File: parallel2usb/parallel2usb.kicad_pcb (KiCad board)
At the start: 4 copper layers, 87.9 x 53.6 mm, 49 parts, among them J1 DB25_Male_MountingHoles, J2 Conn_01x20, J3 Conn_01x03_Male, U1 SN74LVC8T245PW, U2 SN74LVC8T245PW, U3 SN74LVC8T245PW, U4 Pico

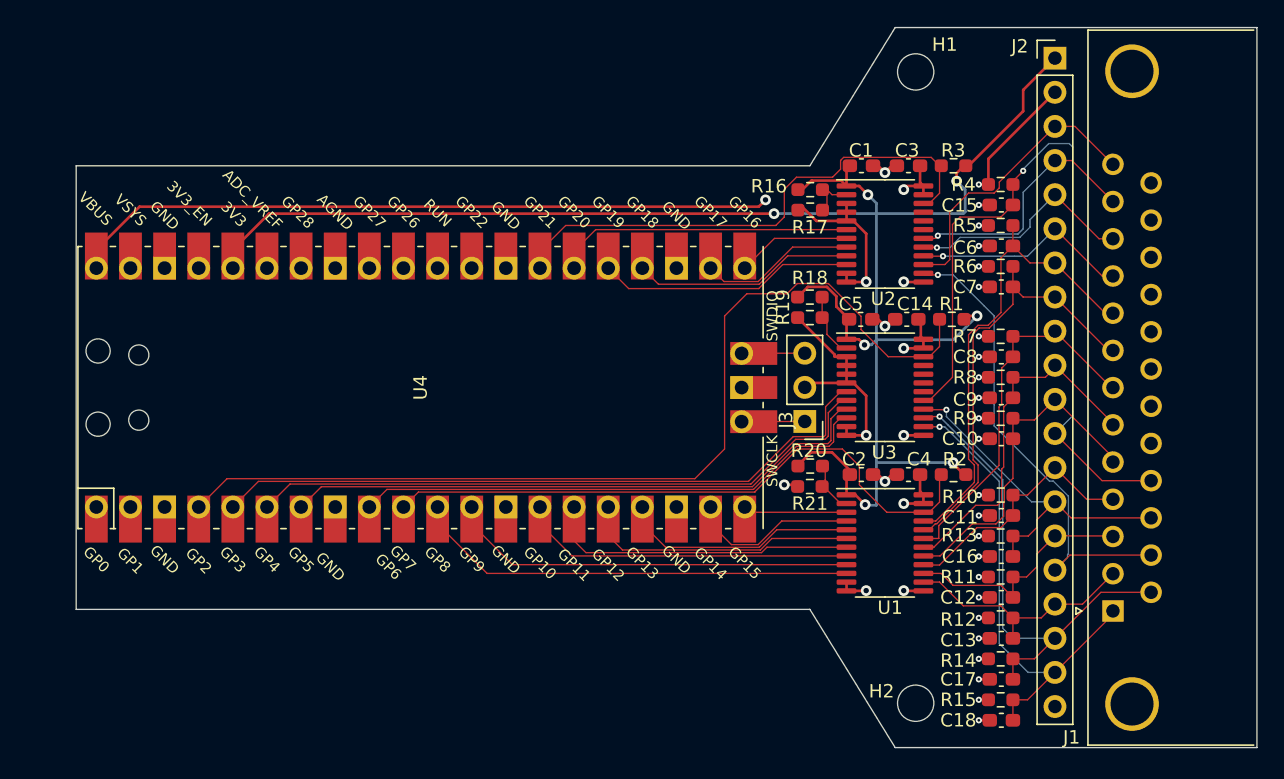
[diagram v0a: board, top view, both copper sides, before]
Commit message: Design with 74LVC161284.
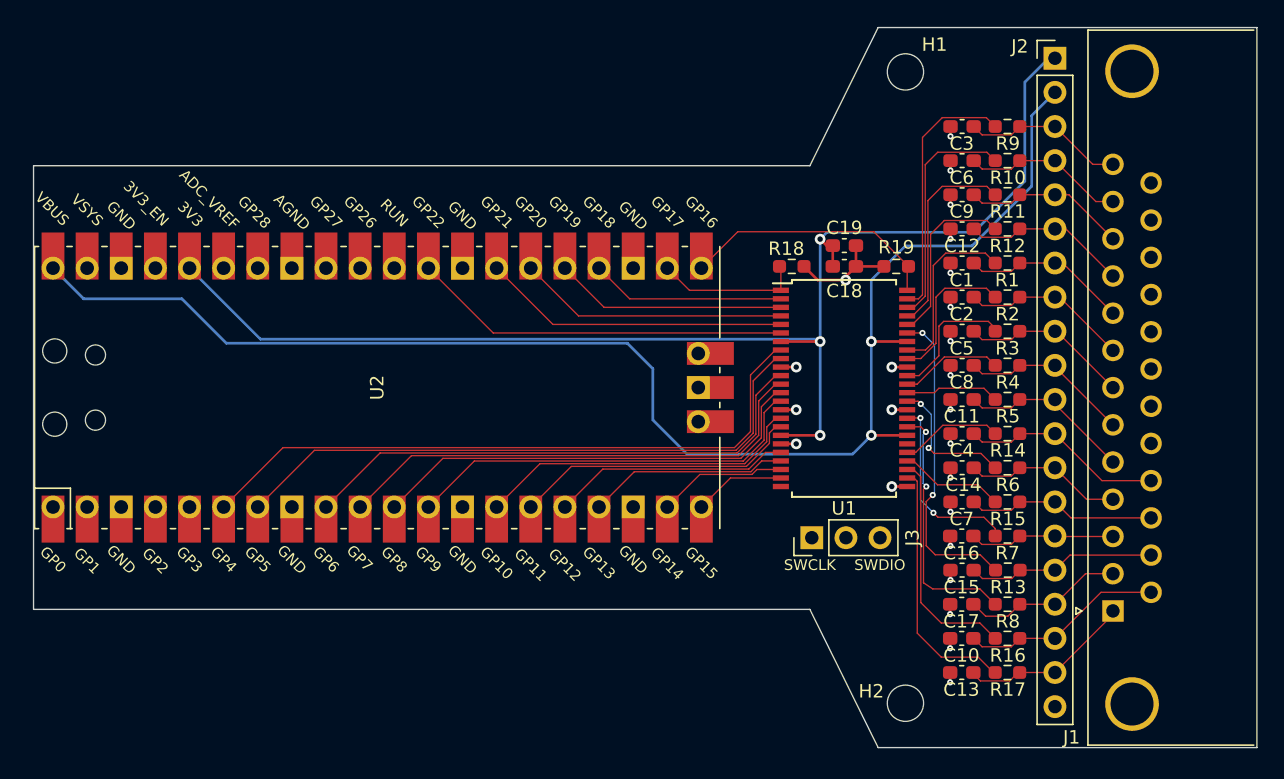
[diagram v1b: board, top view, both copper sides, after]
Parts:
- removed R20: NS, Resistor_SMD:R_0603_1608Metric_Pad0.98x0.95mm_HandSolder
- removed R21: 4K7, Resistor_SMD:R_0603_1608Metric_Pad0.98x0.95mm_HandSolder
- removed U3: SN74LVC8T245PW, Package_SO:TSSOP-24_4.4x7.8mm_P0.65mm
- removed U4: Pico, Raspberry Pico:RPi_Pico_SMD_TH
- added C19: 22u, Capacitor_SMD:C_0603_1608Metric_Pad1.08x0.95mm_HandSolder, F.Cu at (179.1, 91.0)
- C1, C10, C11, C12, C13, C14, C15, C16, C17, C2, C3, C4, C5, C6, C7, C8, C9: value 100n -> 100p
- R1, R10, R11, R12, R13, R14, R15, R16, R2, R3, R4, R5, R6, R7, R8, R9: value 4K7 -> 22
- R17: value NS -> 22
- R18: value NS -> 4K7
- U1: value SN74LVC8T245PW -> 74LVC161284DL; footprint Package_SO:TSSOP-24_4.4x7.8mm_P0.65mm -> Package_SO:SSOP-48_7.5x15.9mm_P0.635mm
- U2: value SN74LVC8T245PW -> Pico; footprint Package_SO:TSSOP-24_4.4x7.8mm_P0.65mm -> RPi_Pico:RPi_Pico_SMD_TH
- moved U2 39.5 mm to (144.3, 101.6), turned to 90 degrees
- moved R17 37.4 mm to (191.2, 122.8)
- moved R16 36.5 mm to (191.2, 120.3), turned to 180 degrees
- moved C18 35.7 mm to (179.1, 92.6), turned to 0 degrees
- moved R12 29.0 mm to (191.2, 89.8), turned to 180 degrees
- moved R11 28.5 mm to (191.2, 87.2), turned to 180 degrees
- moved C12 27.6 mm to (187.9, 89.8)
- moved C15 27.3 mm to (187.9, 115.2)
- moved R10 24.9 mm to (191.2, 84.7), turned to 180 degrees
- moved R9 21.7 mm to (191.2, 82.2), turned to 180 degrees
- moved R8 16.9 mm to (191.2, 117.7), turned to 180 degrees
- moved R14 16.8 mm to (191.2, 105.0), turned to 180 degrees
- moved C7 16.3 mm to (187.9, 110.1)
- moved C9 15.4 mm to (187.9, 87.2)
- moved C2 15.2 mm to (187.9, 94.9), turned to 180 degrees
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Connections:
- C1 pad 1: +3.3V -> /D7
- C10 pad 1: /D3 -> /AUTOF
- C11 pad 1: /D2 -> /D3
- C12 pad 1: /D1 -> /ACK
- C13 pad 1: /D0 -> /STROBE
- C14 pad 1: +5V -> /D2
- C15 pad 1: /SELIN -> /ERROR
- C16 pad 1: /INIT -> /D1
- C17 pad 1: /AUTOF -> /D0
- C18 pad 1: /STROBE -> Vcc
- C2 pad 1: +3.3V -> /D6
- C3 pad 1: +5V -> /SEL
- C4 pad 1: +5V -> /SELIN
- C5 pad 1: +3.3V -> /D5
- C6 pad 1: /D7 -> /PE
- C7 pad 1: /D6 -> /INIT
- C8 pad 1: /D5 -> /D4
- C9 pad 1: /D4 -> /BUSY
- J2 pad 1: +3.3V -> Vcc
- J2 pad 2: +5V -> Vcc_Cable
- R1 pad 1: +3.3V -> /D7
- R1 pad 2: /COEN_3 -> Net-(U1-Pad41)
- R10 pad 1: +5V -> /PE
- R10 pad 2: /D2 -> Net-(U1-Pad46)
- R11 pad 1: +5V -> /BUSY
- R11 pad 2: /D1 -> Net-(U1-Pad45)
- R12 pad 1: +5V -> /ACK
- R12 pad 2: /D0 -> Net-(U1-Pad44)
- R13 pad 1: +5V -> /ERROR
- R13 pad 2: /INIT -> Net-(U1-Pad43)
- R14 pad 1: +5V -> /SELIN
- R14 pad 2: /AUTOF -> Net-(U1-Pad29)
- R15 pad 1: +5V -> /INIT
- R15 pad 2: /STROBE -> Net-(U1-Pad28)
- R16 pad 1: +3.3V -> /AUTOF
- R16 pad 2: /SDIR_3 -> Net-(U1-Pad27)
- R17 pad 1: /SDIR_3 -> /STROBE
- R17 pad 2: GND -> Net-(U1-Pad26)
- R18 pad 1: +3.3V -> GND
- R18 pad 2: /CDIR_3 -> /HD
- R19 pad 1: /CDIR_3 -> GND
- R19 pad 2: GND -> /DIR
- R2 pad 1: +3.3V -> /D6
- R2 pad 2: /DOEN_3 -> Net-(U1-Pad40)
- R3 pad 1: +3.3V -> /D5
- R3 pad 2: /SOEN_3 -> Net-(U1-Pad38)
- R4 pad 1: +5V -> /D4
- R4 pad 2: /SELIN -> Net-(U1-Pad37)
- R5 pad 1: +5V -> /D3
- R5 pad 2: /D7 -> Net-(U1-Pad36)
- R6 pad 1: +5V -> /D2
- R6 pad 2: /D6 -> Net-(U1-Pad35)
- R7 pad 1: +5V -> /D1
- R7 pad 2: /D5 -> Net-(U1-Pad33)
- R8 pad 1: +5V -> /D0
- R8 pad 2: /D4 -> Net-(U1-Pad32)
- R9 pad 1: +5V -> /SEL
- R9 pad 2: /D3 -> Net-(U1-Pad47)
- U1 pad 1: +3.3V -> /HD
- U1 pad 10: /D0_3 -> GND
- U1 pad 11: GND -> /D5_3
- U1 pad 12: GND -> /D4_3
- U1 pad 13: GND -> /D3_3
- U1 pad 14: /D0 -> /D2_3
- U1 pad 15: /D1 -> GND
- U1 pad 16: /D2 -> /D1_3
- U1 pad 17: /D3 -> /D0_3
- U1 pad 18: /D4 -> Vcc
- U1 pad 19: /D5 -> GND
- U1 pad 2: /DDIR_3 -> /SEL_3
- U1 pad 20: /D6 -> /SELIN_3
- U1 pad 21: /D7 -> /INIT_3
- U1 pad 22: /DOEN_3 -> /AUTOF_3
- U1 pad 23: +5V -> /STROBE_3
- U1 pad 24: +5V -> unconnected-(U1-Pad24)
- U1 pad 3: /D7_3 -> /PE_3
- U1 pad 4: /D6_3 -> /BUSY_3
- U1 pad 5: /D5_3 -> /ACK_3
- U1 pad 6: /D4_3 -> /ERROR_3
- U1 pad 7: /D3_3 -> Vcc
- U1 pad 8: /D2_3 -> /D7_3
- U1 pad 9: /D1_3 -> /D6_3
- U2 pad 1: +3.3V -> unconnected-(U2-Pad1)
- U2 pad 10: /ERROR_3 -> /D4_3
- U2 pad 11: GND -> /D3_3
- U2 pad 12: GND -> /D2_3
- U2 pad 14: /ERROR -> /D1_3
- U2 pad 15: /SEL -> /D0_3
- U2 pad 16: /ACK -> /SELIN_3
- U2 pad 17: /BUSY -> /INIT_3
- U2 pad 18: /PE -> GND
- U2 pad 19: unconnected-(U2-Pad19) -> /AUTOF_3
- U2 pad 2: /SDIR_3 -> unconnected-(U2-Pad2)
- U2 pad 20: unconnected-(U2-Pad20) -> /STROBE_3
- U2 pad 21: unconnected-(U2-Pad21) -> /DIR
- U2 pad 22: /SOEN_3 -> /HD
- U2 pad 23: +5V -> GND
- U2 pad 24: +5V -> /SEL_3
- U2 pad 4: GND -> unconnected-(U2-Pad4)
- U2 pad 5: GND -> unconnected-(U2-Pad5)
- U2 pad 6: /ACK_3 -> /D7_3
- U2 pad 7: /BUSY_3 -> /D6_3
- U2 pad 8: /PE_3 -> GND
- U2 pad 9: /SEL_3 -> /D5_3
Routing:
- net +5V: track 171.9 -> 0.00 mm, vias 16 -> 0
- net +3.3V: track 137.5 -> 0.00 mm, vias 7 -> 0
- net Vcc_Cable: track 0.00 -> 108.9 mm, vias 0 -> 2
- net Vcc: track 0.00 -> 99.7 mm, vias 0 -> 3
- net /COEN_3: track 73.0 -> 0.00 mm
- net /DOEN_3: track 46.8 -> 0.00 mm
- net GND: track 379.4 -> 335.4 mm, vias 22 -> 24
- net /SELIN: track 57.4 -> 15.2 mm, vias 1 -> 0
- net /D7_3: track 7.74 -> 48.8 mm
- net /SOEN_3: track 39.3 -> 0.00 mm
- net /AUTOF_3: track 44.6 -> 9.61 mm
- net /D6_3: track 12.7 -> 45.8 mm
- net /SELIN_3: track 50.5 -> 17.8 mm
- net /INIT_3: track 47.4 -> 15.0 mm
- net /STROBE_3: track 39.0 -> 6.81 mm
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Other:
- board size 87.9 x 53.6 mm -> 91.1 x 53.6 mm
